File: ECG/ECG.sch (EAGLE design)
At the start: 30 parts, among them U2 AD8232

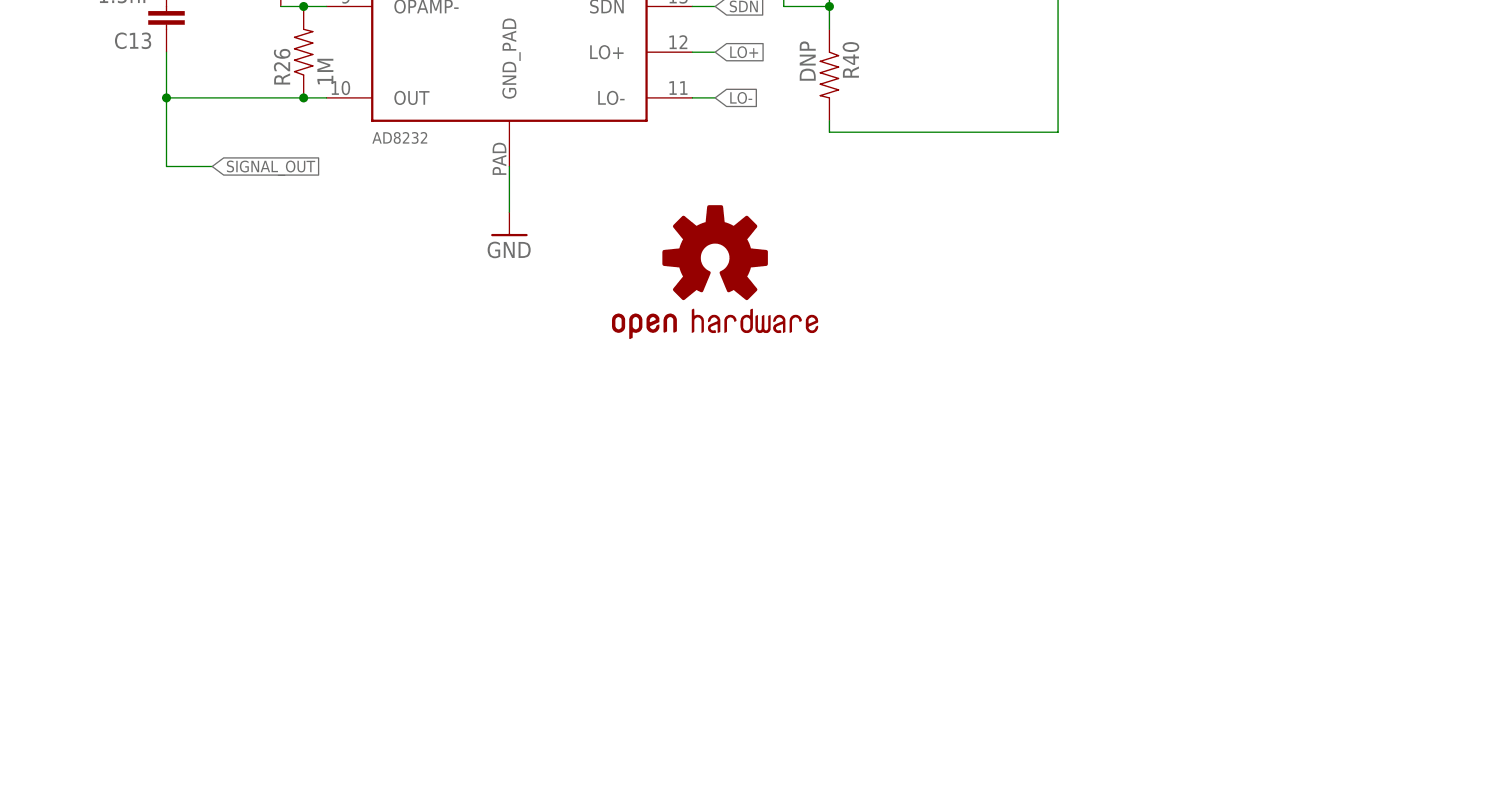
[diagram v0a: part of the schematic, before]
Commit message: Added BGM111
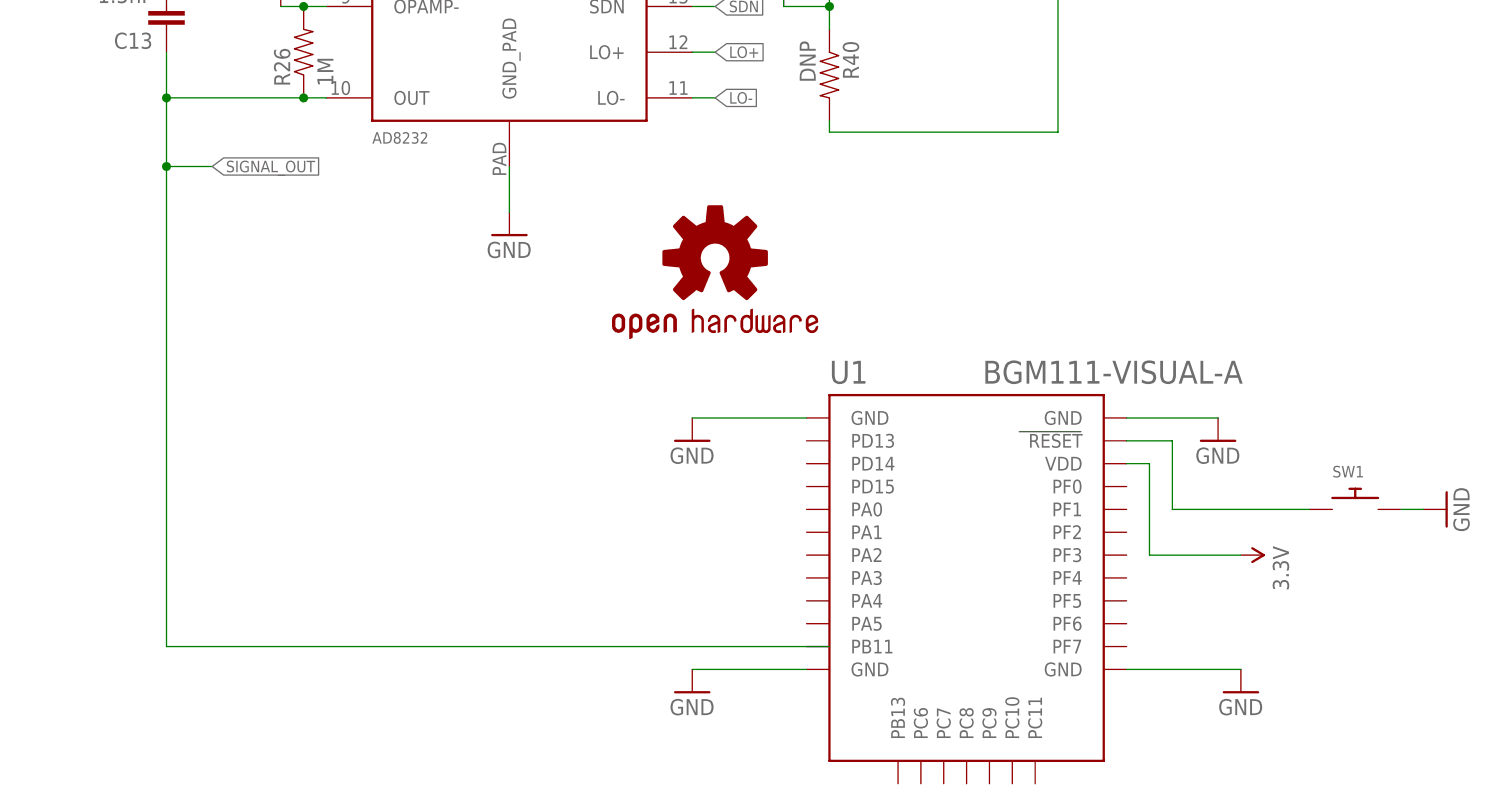
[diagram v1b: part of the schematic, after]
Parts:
- added SW1: (no value), adafruit:SWITCH_PUSHBUTTONSOFTTOUCHSMD_SJ
- added U1: BGM111-VISUAL-A, sf-bluegiga:BGM111-VISUAL-A
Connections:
- new net N$1: SW1.P$1, U1.RESET
- net 3.3V: now also U1.VDD
- net GND: now also SW1.P$2, U1.GND, U1.GND@2, U1.GND@3, U1.GND@4
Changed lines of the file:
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@@
 <layer number="54" name="bGND_GNDA" color="1" fill="9" visible="no" active="no"/>
 <layer number="56" name="wert" color="7" fill="1" visible="no" active="no"/>
+<layer number="57" name="tCAD" color="7" fill="1" visible="no" active="no"/>
+<layer number="59" name="Invisible" color="7" fill="1" visible="no" active="no"/>
+<layer number="60" name="bCarbon" color="7" fill="1" visible="no" active="no"/>
+<layer number="61" name="stand" color="7" fill="1" visible="no" active="no"/>
+<layer number="90" name="Modules" color="5" fill="1" visible="yes" active="yes"/>
 <layer number="91" name="Nets" color="2" fill="1" visible="yes" active="yes"/>
 <layer number="92" name="Busses" color="1" fill="1" visible="yes" active="yes"/>
@@
 <layer number="97" name="Info" color="7" fill="1" visible="yes" active="yes"/>
 <layer number="98" name="Guide" color="6" fill="1" visible="yes" active="yes"/>
+<layer number="99" name="Invisibles" color="7" fill="1" visible="no" active="no"/>
 <layer number="100" name="Muster" color="7" fill="1" visible="no" active="no"/>
 <layer number="101" name="Patch_Top" color="12" fill="4" visible="yes" active="yes"/>
@@
 <layer number="108" name="tplace-old" color="10" fill="1" visible="yes" active="yes"/>
 <layer number="109" name="ref-old" color="11" fill="1" visible="yes" active="yes"/>
+<layer number="110" name="fp0" color="7" fill="1" visible="yes" active="yes"/>
+<layer number="111" name="Text" color="7" fill="1" visible="yes" active="yes"/>
+<layer number="112" name="2Restrict" color="7" fill="1" visible="yes" active="yes"/>
+<layer number="113" name="IDFDebug" color="4" fill="1" visible="yes" active="yes"/>
 <layer number="116" name="Patch_BOT" color="9" fill="4" visible="no" active="yes"/>
+<layer number="118" name="Rect_Pads" color="7" fill="1" visible="no" active="no"/>
 <layer number="121" name="_tsilk" color="7" fill="1" visible="no" active="yes"/>
 <layer number="122" name="_bsilk" color="7" fill="1" visible="no" active="yes"/>
+<layer number="123" name="tTestmark" color="7" fill="1" visible="yes" active="yes"/>
+<layer number="124" name="bTestmark" color="7" fill="1" visible="yes" active="yes"/>
 <layer number="125" name="_tNames" color="7" fill="1" visible="no" active="yes"/>
+<layer number="126" name="_bNames" color="7" fill="1" visible="yes" active="yes"/>
+<layer number="127" name="_tValues" color="7" fill="1" visible="yes" active="yes"/>
+<layer number="128" name="_bValues" color="7" fill="1" visible="yes" active="yes"/>
+<layer number="129" name="Mask" color="7" fill="1" visible="yes" active="yes"/>
+<layer number="130" name="bLogo" color="7" fill="1" visible="yes" active="yes"/>
+<layer number="131" name="tText" color="7" fill="1" visible="yes" active="yes"/>
+<layer number="132" name="bMask" color="7" fill="1" visible="yes" active="yes"/>
 <layer number="144" name="Drill_legend" color="7" fill="1" visible="no" active="yes"/>
+<layer number="150" name="Notes" color="7" fill="1" visible="yes" active="yes"/>
 <layer number="151" name="HeatSink" color="7" fill="1" visible="no" active="yes"/>
+<layer number="152" name="_bDocu" color="7" fill="1" visible="yes" active="yes"/>
+<layer number="153" name="FabDoc1" color="7" fill="1" visible="yes" active="yes"/>
+<layer number="154" name="FabDoc2" color="7" fill="1" visible="yes" active="yes"/>
+<layer number="155" name="FabDoc3" color="7" fill="1" visible="yes" active="yes"/>
 <layer number="199" name="Contour" color="7" fill="1" visible="no" active="yes"/>
 <layer number="200" name="200bmp" color="1" fill="10" visible="no" active="yes"/>
@@
 <layer number="223" name="223bmp" color="24" fill="1" visible="no" active="no"/>
 <layer number="224" name="224bmp" color="25" fill="1" visible="no" active="no"/>
+<layer number="225" name="225bmp" color="7" fill="1" visible="yes" active="yes"/>
+<layer number="226" name="226bmp" color="7" fill="1" visible="yes" active="yes"/>
+<layer number="227" name="227bmp" color="7" fill="1" visible="yes" active="yes"/>
+<layer number="228" name="228bmp" color="7" fill="1" visible="yes" active="yes"/>
+<layer number="229" name="229bmp" color="7" fill="1" visible="yes" active="yes"/>
+<layer number="230" name="230bmp" color="7" fill="1" visible="yes" active="yes"/>
+<layer number="231" name="Eagle3D_PG1" color="14" fill="1" visible="yes" active="yes"/>
+<layer number="232" name="Eagle3D_PG2" color="14" fill="2" visible="yes" active="yes"/>
+<layer number="233" name="Eagle3D_PG3" color="14" fill="4" visible="yes" active="yes"/>
+<layer number="248" name="Housing" color="7" fill="1" visible="yes" active="yes"/>
+<layer number="249" name="Edge" color="7" fill="1" visible="yes" active="yes"/>
 <layer number="250" name="Descript" color="3" fill="1" visible="no" active="no"/>
 <layer number="251" name="SMDround" color="12" fill="11" visible="no" active="no"/>
 <layer number="254" name="cooling" color="7" fill="1" visible="no" active="yes"/>
+<layer number="255" name="routoute" color="7" fill="1" visible="yes" active="yes"/>
 </layers>
 <schematic xreflabel="%F%N/%S.%C%R" xrefpart="/%S.%C%R">
@@
 <part name="R40" library="SparkFun-Resistors" deviceset="0OHM1/10W5%(0603)" device="" value="DNP"/>
 <part name="LOGO3" library="SparkFun-Aesthetics" deviceset="OSHW-LOGO" device="S"/>
+<part name="U1" library="sf-bluegiga" deviceset="BGM111-VISUAL" device="-A"/>
+<part name="GND1" library="SparkFun-Aesthetics" deviceset="GND" device=""/>
+<part name="GND2" library="SparkFun-Aesthetics" deviceset="GND" device=""/>
+<part name="GND3" library="SparkFun-Aesthetics" deviceset="GND" device=""/>
+<part name="GND4" library="SparkFun-Aesthetics" deviceset="GND" device=""/>
+<part name="SUPPLY2" library="SparkFun-Aesthetics" deviceset="3.3V" device=""/>
+<part name="SW1" library="adafruit" deviceset="SWITCH_PUSHBUTTON" device="SOFTTOUCHSMD_SJ"/>
+<part name="GND8" library="SparkFun-Aesthetics" deviceset="GND" device=""/>
 </parts>
 <sheets>
@@
 <instance part="R40" gate="G$1" x="162.56" y="-20.32" rot="R270"/>
 <instance part="LOGO3" gate="G$1" x="149.86" y="-40.64"/>
+<instance part="U1" gate="G$1" x="177.8" y="-76.2"/>
+<instance part="GND1" gate="1" x="147.32" y="-60.96"/>
+<instance part="GND2" gate="1" x="147.32" y="-88.9"/>
+<instance part="GND3" gate="1" x="208.28" y="-88.9"/>
+<instance part="GND4" gate="1" x="205.74" y="-60.96"/>
+<instance part="SUPPLY2" gate="G$1" x="208.28" y="-73.66" rot="R270"/>
+<instance part="SW1" gate="G$1" x="220.98" y="-68.58"/>
+<instance part="GND8" gate="1" x="231.14" y="-68.58" rot="R90"/>
 </instances>
 <busses>
@@
 <wire x1="10.16" y1="0" x2="10.16" y2="2.54" width="0.1524" layer="91"/>
 </segment>
+<segment>
+<pinref part="U1" gate="G$1" pin="GND"/>
+<pinref part="GND1" gate="1" pin="GND"/>
+<wire x1="160.02" y1="-58.42" x2="147.32" y2="-58.42" width="0.1524" layer="91"/>
+</segment>
+<segment>
+<pinref part="U1" gate="G$1" pin="GND@2"/>
+<pinref part="GND2" gate="1" pin="GND"/>
+<wire x1="160.02" y1="-86.36" x2="147.32" y2="-86.36" width="0.1524" layer="91"/>
+</segment>
+<segment>
+<pinref part="U1" gate="G$1" pin="GND@3"/>
+<pinref part="GND3" gate="1" pin="GND"/>
+<wire x1="195.58" y1="-86.36" x2="208.28" y2="-86.36" width="0.1524" layer="91"/>
+</segment>
+<segment>
+<pinref part="U1" gate="G$1" pin="GND@4"/>
+<pinref part="GND4" gate="1" pin="GND"/>
+<wire x1="195.58" y1="-58.42" x2="205.74" y2="-58.42" width="0.1524" layer="91"/>
+</segment>
+<segment>
+<pinref part="GND8" gate="1" pin="GND"/>
+<pinref part="SW1" gate="G$1" pin="P$2"/>
+<wire x1="228.6" y1="-68.58" x2="226.06" y2="-68.58" width="0.1524" layer="91"/>
+</segment>
 </net>
 <net name="N$12" class="0">
@@
 <label x="93.98" y="-30.48" size="1.27" layer="95" xref="yes"/>
 <junction x="88.9" y="-22.86"/>
+<wire x1="88.9" y1="-30.48" x2="88.9" y2="-83.82" width="0.1524" layer="91"/>
+<junction x="88.9" y="-30.48"/>
+<wire x1="88.9" y1="-83.82" x2="162.56" y2="-83.82" width="0.1524" layer="91"/>
 </segment>
 <segment>
@@
 <wire x1="27.94" y1="17.78" x2="27.94" y2="15.24" width="0.1524" layer="91"/>
 </segment>
+<segment>
+<pinref part="U1" gate="G$1" pin="VDD"/>
+<wire x1="195.58" y1="-63.5" x2="198.12" y2="-63.5" width="0.1524" layer="91"/>
+<wire x1="198.12" y1="-63.5" x2="198.12" y2="-73.66" width="0.1524" layer="91"/>
+<wire x1="198.12" y1="-73.66" x2="208.28" y2="-73.66" width="0.1524" layer="91"/>
+<pinref part="SUPPLY2" gate="G$1" pin="3.3V"/>
+</segment>
 </net>
 <net name="LO+" class="0">
@@
 </segment>
 </net>
+<net name="N$1" class="0">
+<segment>
+<pinref part="U1" gate="G$1" pin="RESET"/>
+<wire x1="195.58" y1="-60.96" x2="200.66" y2="-60.96" width="0.1524" layer="91"/>
+<wire x1="200.66" y1="-60.96" x2="200.66" y2="-68.58" width="0.1524" layer="91"/>
+<pinref part="SW1" gate="G$1" pin="P$1"/>
+<wire x1="200.66" y1="-68.58" x2="215.9" y2="-68.58" width="0.1524" layer="91"/>
+</segment>
+</net>

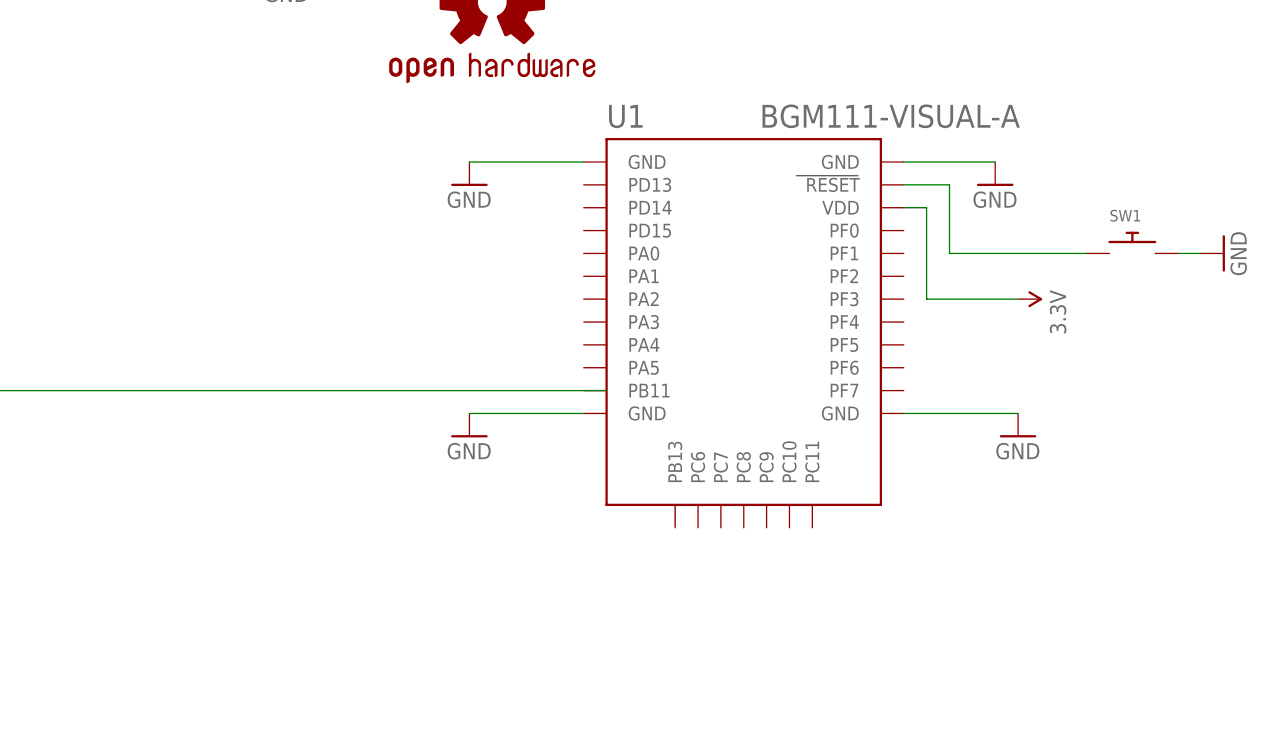
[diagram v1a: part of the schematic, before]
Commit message: Added Tag Connector for Programming/Debugging BGM111
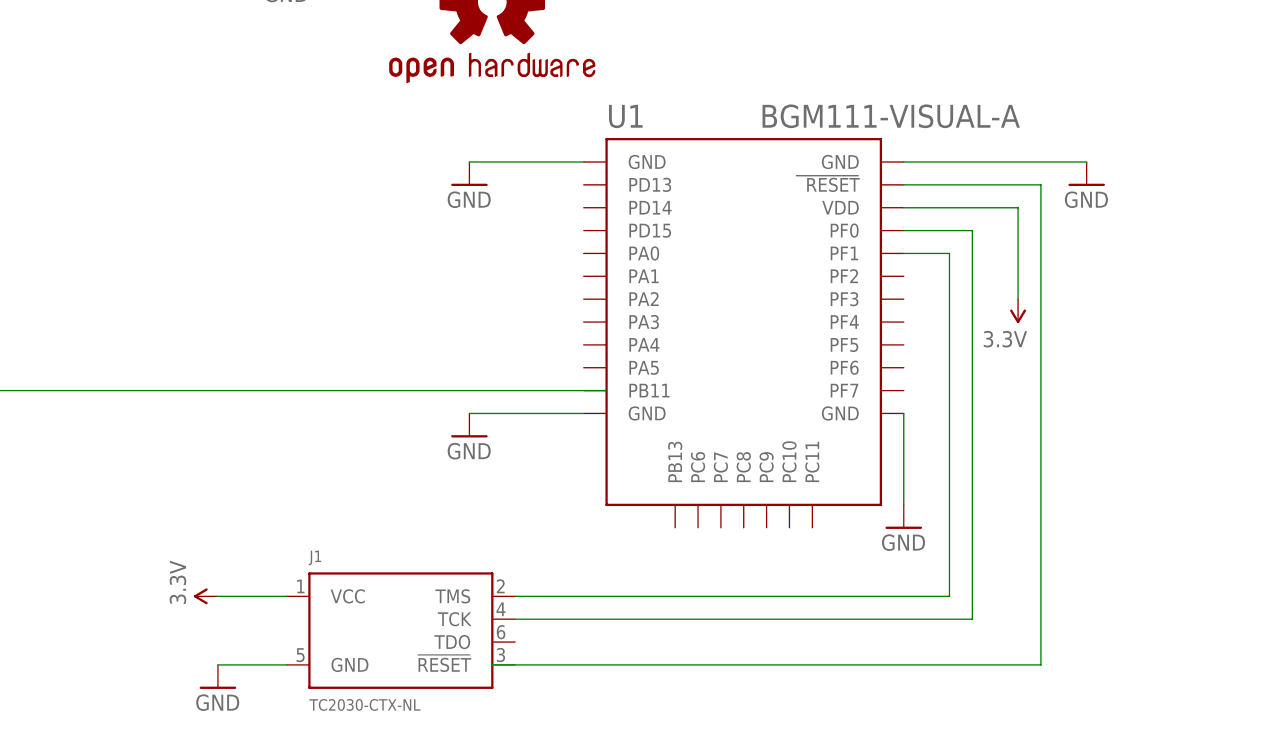
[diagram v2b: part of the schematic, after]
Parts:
- removed SW1: (no value), adafruit:SWITCH_PUSHBUTTONSOFTTOUCHSMD_SJ
- added J1: TC2030-CTX-NL, tag_connector:TC2030-CTX-NL
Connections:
- removed net N$1: SW1.P$1, U1.RESET
- new net N$2: U1.RESET
- new net N$3: J1.TCK, U1.PF0
- new net N$4: J1.TMS, U1.PF1
- net 3.3V: now also J1.VCC
- net GND: now also J1.GND; no longer SW1.P$2
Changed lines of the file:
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@@
 <part name="GND4" library="SparkFun-Aesthetics" deviceset="GND" device=""/>
 <part name="SUPPLY2" library="SparkFun-Aesthetics" deviceset="3.3V" device=""/>
-<part name="SW1" library="adafruit" deviceset="SWITCH_PUSHBUTTON" device="SOFTTOUCHSMD_SJ"/>
 <part name="GND8" library="SparkFun-Aesthetics" deviceset="GND" device=""/>
+<part name="J1" library="tag_connector" deviceset="TC2030-CTX" device="-NL"/>
+<part name="SUPPLY1" library="SparkFun-Aesthetics" deviceset="3.3V" device=""/>
 </parts>
 <sheets>
@@
 <instance part="GND1" gate="1" x="147.32" y="-60.96"/>
 <instance part="GND2" gate="1" x="147.32" y="-88.9"/>
-<instance part="GND3" gate="1" x="208.28" y="-88.9"/>
-<instance part="GND4" gate="1" x="205.74" y="-60.96"/>
-<instance part="SUPPLY2" gate="G$1" x="208.28" y="-73.66" rot="R270"/>
-<instance part="SW1" gate="G$1" x="220.98" y="-68.58"/>
-<instance part="GND8" gate="1" x="231.14" y="-68.58" rot="R90"/>
+<instance part="GND3" gate="1" x="195.58" y="-99.06"/>
+<instance part="GND4" gate="1" x="215.9" y="-60.96"/>
+<instance part="SUPPLY2" gate="G$1" x="208.28" y="-73.66" rot="R180"/>
+<instance part="GND8" gate="1" x="119.38" y="-116.84"/>
+<instance part="J1" gate="G$1" x="139.7" y="-109.22"/>
+<instance part="SUPPLY1" gate="G$1" x="119.38" y="-106.68" rot="R90"/>
 </instances>
 <busses>
@@
 <pinref part="U1" gate="G$1" pin="GND@3"/>
 <pinref part="GND3" gate="1" pin="GND"/>
-<wire x1="195.58" y1="-86.36" x2="208.28" y2="-86.36" width="0.1524" layer="91"/>
+<wire x1="195.58" y1="-86.36" x2="195.58" y2="-96.52" width="0.1524" layer="91"/>
 </segment>
 <segment>
 <pinref part="U1" gate="G$1" pin="GND@4"/>
 <pinref part="GND4" gate="1" pin="GND"/>
-<wire x1="195.58" y1="-58.42" x2="205.74" y2="-58.42" width="0.1524" layer="91"/>
+<wire x1="195.58" y1="-58.42" x2="215.9" y2="-58.42" width="0.1524" layer="91"/>
 </segment>
 <segment>
 <pinref part="GND8" gate="1" pin="GND"/>
-<pinref part="SW1" gate="G$1" pin="P$2"/>
-<wire x1="228.6" y1="-68.58" x2="226.06" y2="-68.58" width="0.1524" layer="91"/>
+<pinref part="J1" gate="G$1" pin="GND"/>
+<wire x1="119.38" y1="-114.3" x2="127" y2="-114.3" width="0.1524" layer="91"/>
 </segment>
 </net>
@@
 </segment>
 <segment>
+<pinref part="SUPPLY1" gate="G$1" pin="3.3V"/>
+<pinref part="J1" gate="G$1" pin="VCC"/>
+<wire x1="119.38" y1="-106.68" x2="127" y2="-106.68" width="0.1524" layer="91"/>
+</segment>
+<segment>
 <pinref part="U1" gate="G$1" pin="VDD"/>
-<wire x1="195.58" y1="-63.5" x2="198.12" y2="-63.5" width="0.1524" layer="91"/>
-<wire x1="198.12" y1="-63.5" x2="198.12" y2="-73.66" width="0.1524" layer="91"/>
-<wire x1="198.12" y1="-73.66" x2="208.28" y2="-73.66" width="0.1524" layer="91"/>
+<wire x1="195.58" y1="-63.5" x2="208.28" y2="-63.5" width="0.1524" layer="91"/>
+<wire x1="208.28" y1="-63.5" x2="208.28" y2="-73.66" width="0.1524" layer="91"/>
 <pinref part="SUPPLY2" gate="G$1" pin="3.3V"/>
 </segment>
@@
 </segment>
 </net>
-<net name="N$1" class="0">
+<net name="N$4" class="0">
+<segment>
+<pinref part="U1" gate="G$1" pin="PF1"/>
+<wire x1="195.58" y1="-68.58" x2="200.66" y2="-68.58" width="0.1524" layer="91"/>
+<pinref part="J1" gate="G$1" pin="TMS"/>
+<wire x1="152.4" y1="-106.68" x2="200.66" y2="-106.68" width="0.1524" layer="91"/>
+<wire x1="200.66" y1="-106.68" x2="200.66" y2="-68.58" width="0.1524" layer="91"/>
+</segment>
+</net>
+<net name="N$3" class="0">
+<segment>
+<pinref part="U1" gate="G$1" pin="PF0"/>
+<wire x1="195.58" y1="-66.04" x2="203.2" y2="-66.04" width="0.1524" layer="91"/>
+<wire x1="203.2" y1="-66.04" x2="203.2" y2="-109.22" width="0.1524" layer="91"/>
+<pinref part="J1" gate="G$1" pin="TCK"/>
+<wire x1="203.2" y1="-109.22" x2="152.4" y2="-109.22" width="0.1524" layer="91"/>
+</segment>
+</net>
+<net name="N$2" class="0">
 <segment>
 <pinref part="U1" gate="G$1" pin="RESET"/>
-<wire x1="195.58" y1="-60.96" x2="200.66" y2="-60.96" width="0.1524" layer="91"/>
-<wire x1="200.66" y1="-60.96" x2="200.66" y2="-68.58" width="0.1524" layer="91"/>
-<pinref part="SW1" gate="G$1" pin="P$1"/>
-<wire x1="200.66" y1="-68.58" x2="215.9" y2="-68.58" width="0.1524" layer="91"/>
-</segment>
-</net>
+<wire x1="195.58" y1="-60.96" x2="210.82" y2="-60.96" width="0.1524" layer="91"/>
+<wire x1="210.82" y1="-60.96" x2="210.82" y2="-114.3" width="0.1524" layer="91"/>
+<wire x1="210.82" y1="-114.3" x2="149.86" y2="-114.3" width="0.1524" layer="91"/>
+</segment>
+</net>
